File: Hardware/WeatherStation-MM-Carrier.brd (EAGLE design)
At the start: 67.3 x 58.4 mm, 157 parts, among them J11 microSD, J13 RJ11 - WIND, J15 MICROMOD-2222-C, J2 JTAG, J3 QWIIC_RIGHT_ANGLE, J7 RJ11 - RAIN, U1 BME280, U2 VEML6075, U3 AS3935, U5 AP7361C-33FGE

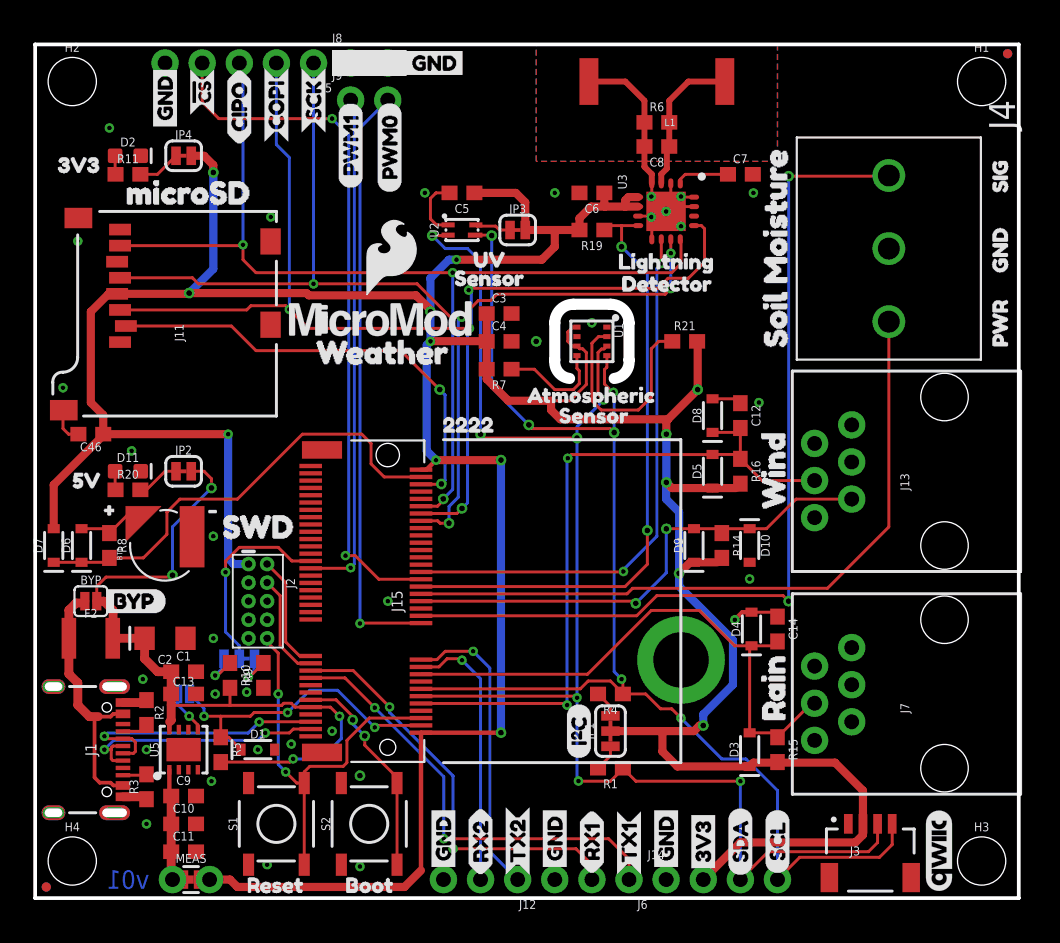
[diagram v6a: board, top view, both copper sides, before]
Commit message: Impelemented design review changes
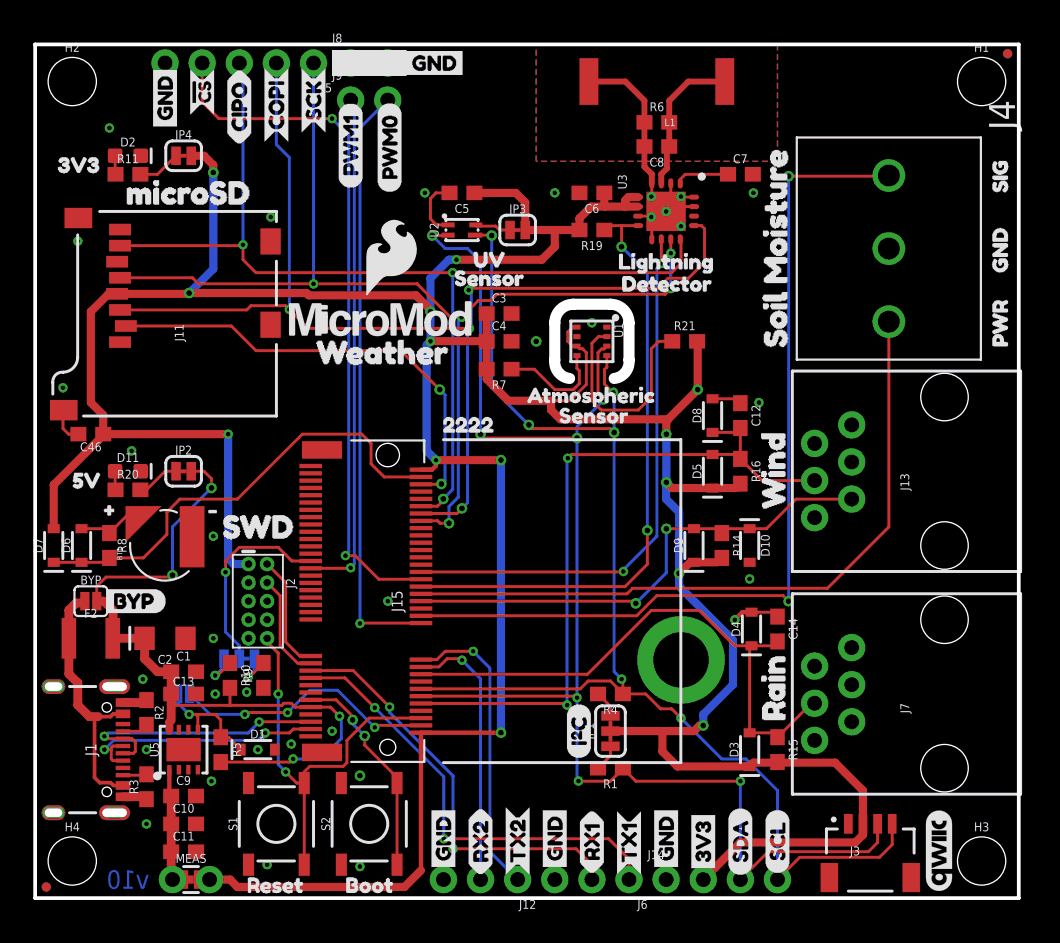
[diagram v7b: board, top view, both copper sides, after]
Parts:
- U5: value AP7361C-33FGE -> AP7361C-33FGEUDFN-8; device ublox:8-UDFN -> SparkFun-IC-Power:UDFN-8
- moved LOGO1 5.08 mm to (33.0, 25.4)
- moved U$68 5.08 mm to (33.0, 21.6)
- moved U$58 5.08 mm to (38.9, 19.1)
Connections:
- net SPI_MISO renamed SPI_CIPO
- net SPI_MOSI renamed SPI_COPI
- new net VREG_EN: D1.C, JP6.2, R5.1, U5.5
- net 3.3V_EN: no longer D1.C, JP6.2, R5.1, U5.5
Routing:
- net VREG_EN: track 0.00 -> 8.04 mm, vias 0 -> 1
- net 3.3V_EN: track 24.8 -> 18.2 mm, vias 4 -> 3
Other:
- board text added: "Priyanka Makin"
- board text added: "v10"
- board text removed: "v01"

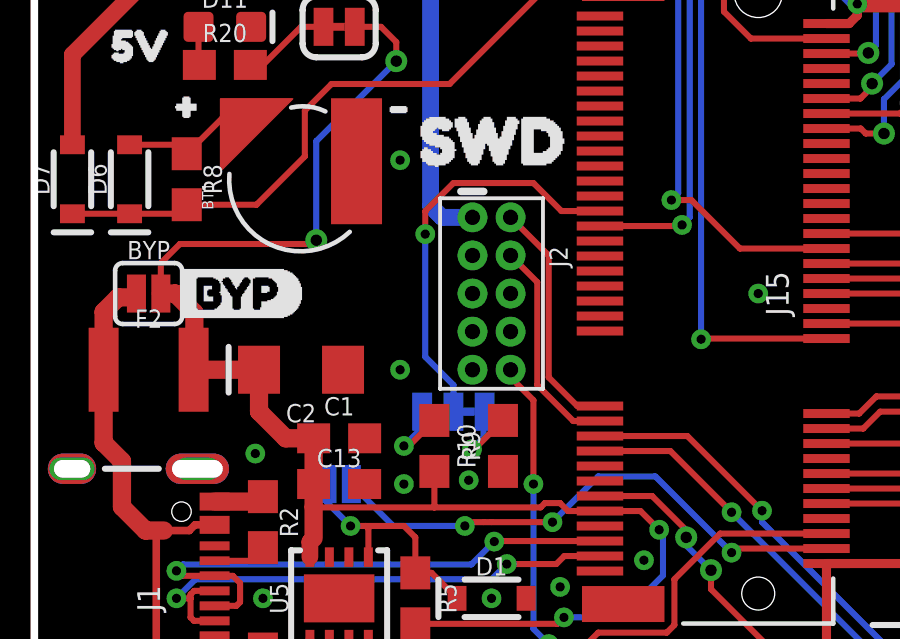
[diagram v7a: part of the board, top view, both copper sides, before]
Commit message: Removed VIN/3 jumper
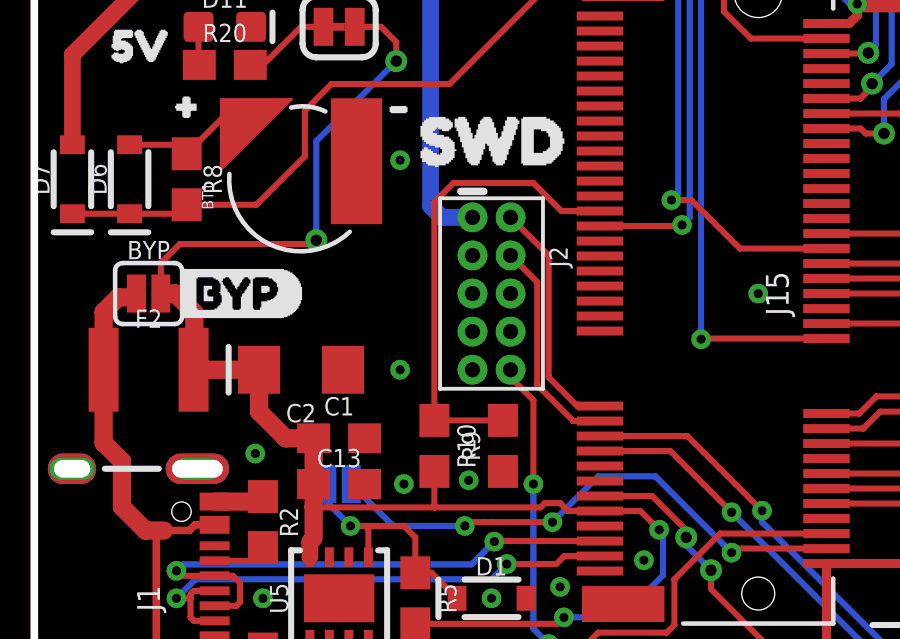
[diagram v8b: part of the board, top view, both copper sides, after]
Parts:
- removed JP5: VIN/3, SparkFun-Jumpers:SMT-JUMPER_3_2-NC_TRACE_SILK
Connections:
- removed net N$12: JP5.1, R9.2
- removed net N$9: JP5.3, R10.1
- net VIN/3: now also R10.1, R9.2; no longer JP5.2
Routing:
- net N$12: track 2.86 -> 0.00 mm, vias 1 -> 0
- net N$9: track 2.76 -> 0.00 mm, vias 1 -> 0
- net VIN/3: track 13.7 -> 15.7 mm, vias 1 -> 0
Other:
- board text added: "Selective Solder Nozzle Width: 0.354331"
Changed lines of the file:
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@@
 <drawing>
 <settings>
-<setting alwaysvectorfont="yes"/>
+<setting alwaysvectorfont="no"/>
 <setting verticaltext="up"/>
 </settings>
@@
 <layer number="46" name="Milling" color="3" fill="1" visible="no" active="yes"/>
 <layer number="47" name="Measures" color="7" fill="1" visible="no" active="yes"/>
-<layer number="48" name="Document" color="7" fill="1" visible="no" active="yes"/>
+<layer number="48" name="Document" color="7" fill="1" visible="yes" active="yes"/>
 <layer number="49" name="Reference" color="7" fill="1" visible="no" active="yes"/>
 <layer number="50" name="dxf" color="7" fill="1" visible="no" active="yes"/>
@@
 <text x="40.64" y="39.37" size="0.254" layer="20" font="vector" ratio="15" rot="R270">ROUTE OUT</text>
 <text x="36.83" y="-21.59" size="1.778" layer="51" font="vector" ratio="15">Priyanka Makin</text>
+<wire x1="58.42" y1="50.8" x2="58.42" y2="40.64" width="9.00000625" layer="48"/>
+<wire x1="58.42" y1="40.64" x2="55.88" y2="35.56" width="9.00000625" layer="48"/>
+<wire x1="55.88" y1="35.56" x2="55.88" y2="12.7" width="9.00000625" layer="48"/>
+<text x="71.12" y="40.64" size="1.778" layer="48" font="vector" ratio="15">Selective Solder Nozzle Width:
+0.354331</text>
 </plain>
 <attributes>
@@
 <attribute name="VALUE" x="33.02" y="44.577" size="0.6096" layer="27" font="vector" ratio="20" align="top-center"/>
 </element>
-<element name="JP5" library="SparkFun-Jumpers" package="SMT-JUMPER_3_2-NC_TRACE_SILK" package3d_urn="urn:adsk.eagle:package:39289/1" value="VIN/3" x="13.97" y="16.383" smashed="yes" rot="MR0">
-<attribute name="NAME" x="13.97" y="17.526" size="0.6096" layer="26" font="vector" ratio="20" rot="MR0" align="bottom-center"/>
-<attribute name="VALUE" x="13.97" y="15.24" size="0.6096" layer="28" font="vector" ratio="20" rot="MR0" align="top-center"/>
-</element>
 <element name="U$44" library="SparkFun-Aesthetics" package="SFE_LOGO_FLAME_.2" value="" x="24.384" y="43.815" smashed="yes"/>
 <element name="U$58" library="buzzard_labels (3)" package="WEATHER4" value="" x="38.862" y="19.05" smashed="yes" rot="MR0"/>
@@
 <contactref element="J15" pad="49"/>
 <wire x1="18.855" y1="23.07" x2="17.57" y2="23.07" width="0.2032" layer="1"/>
-<contactref element="JP5" pad="2"/>
-<wire x1="13.97" y1="16.383" x2="13.97" y2="17.272" width="0.2032" layer="16"/>
-<wire x1="13.030946875" y1="18.211053125" x2="13.030946875" y2="22.301946875" width="0.2032" layer="16"/>
-<via x="13.030946875" y="22.301946875" extent="1-16" drill="0.3048"/>
-<wire x1="13.030946875" y1="22.301946875" x2="13.030946875" y2="23.063946875" width="0.2032" layer="1"/>
-<wire x1="13.97" y1="17.272" x2="13.030946875" y2="18.211053125" width="0.2032" layer="16"/>
-<wire x1="13.030946875" y1="23.063946875" x2="13.97" y2="24.003" width="0.2032" layer="1"/>
+<wire x1="13.335" y1="16.09" x2="13.335" y2="23.368" width="0.2032" layer="1"/>
+<wire x1="13.335" y1="23.368" x2="13.97" y2="24.003" width="0.2032" layer="1"/>
+<contactref element="R9" pad="2"/>
+<contactref element="R10" pad="1"/>
+<wire x1="13.335" y1="16.09" x2="15.621" y2="16.09" width="0.2032" layer="1"/>
 </signal>
 <signal name="N$1">
@@
 <wire x1="30.2433" y1="45.9867" x2="31.5102875" y2="45.9867" width="0.2032" layer="1"/>
 </signal>
-<signal name="N$9">
-<contactref element="JP5" pad="3"/>
-<contactref element="R10" pad="1"/>
-<wire x1="13.335" y1="16.09" x2="12.485" y2="15.24" width="0.2032" layer="1"/>
-<wire x1="12.485" y1="15.24" x2="12.319" y2="15.24" width="0.2032" layer="1"/>
-<via x="12.319" y="15.24" extent="1-16" drill="0.3048"/>
-<wire x1="12.319" y1="15.24" x2="12.9286" y2="15.8496" width="0.2032" layer="16"/>
-<wire x1="12.9286" y1="15.8496" x2="12.9286" y2="16.383" width="0.2032" layer="16"/>
-</signal>
-<signal name="N$12">
-<contactref element="R9" pad="2"/>
-<contactref element="JP5" pad="1"/>
-<wire x1="15.621" y1="16.09" x2="14.658709375" y2="15.127709375" width="0.2032" layer="1"/>
-<wire x1="14.658709375" y1="15.127709375" x2="14.590290625" y2="15.127709375" width="0.2032" layer="1"/>
-<via x="14.590290625" y="15.127709375" extent="1-16" drill="0.3048"/>
-<wire x1="14.590290625" y1="15.127709375" x2="14.971290625" y2="15.508709375" width="0.2032" layer="16"/>
-<wire x1="14.971290625" y1="16.342890625" x2="14.971290625" y2="15.508709375" width="0.2032" layer="16"/>
-<wire x1="14.971290625" y1="16.342890625" x2="15.0114" y2="16.383" width="0.2032" layer="16"/>
-</signal>
 <signal name="VREG_EN">
 <contactref element="U5" pad="5"/>
@@
 </drawing>
 <compatibility>
+<note version="6.3" minversion="6.2.2" severity="warning">
+Since Version 6.2.2 text objects can contain more than one line,
+which will not be processed correctly with this version.
+</note>
 <note version="8.3" severity="warning">
 Since Version 8.3, EAGLE supports URNs for individual library
